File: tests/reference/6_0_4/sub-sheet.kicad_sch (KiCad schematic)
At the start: 7 parts, among them U1 74LS04

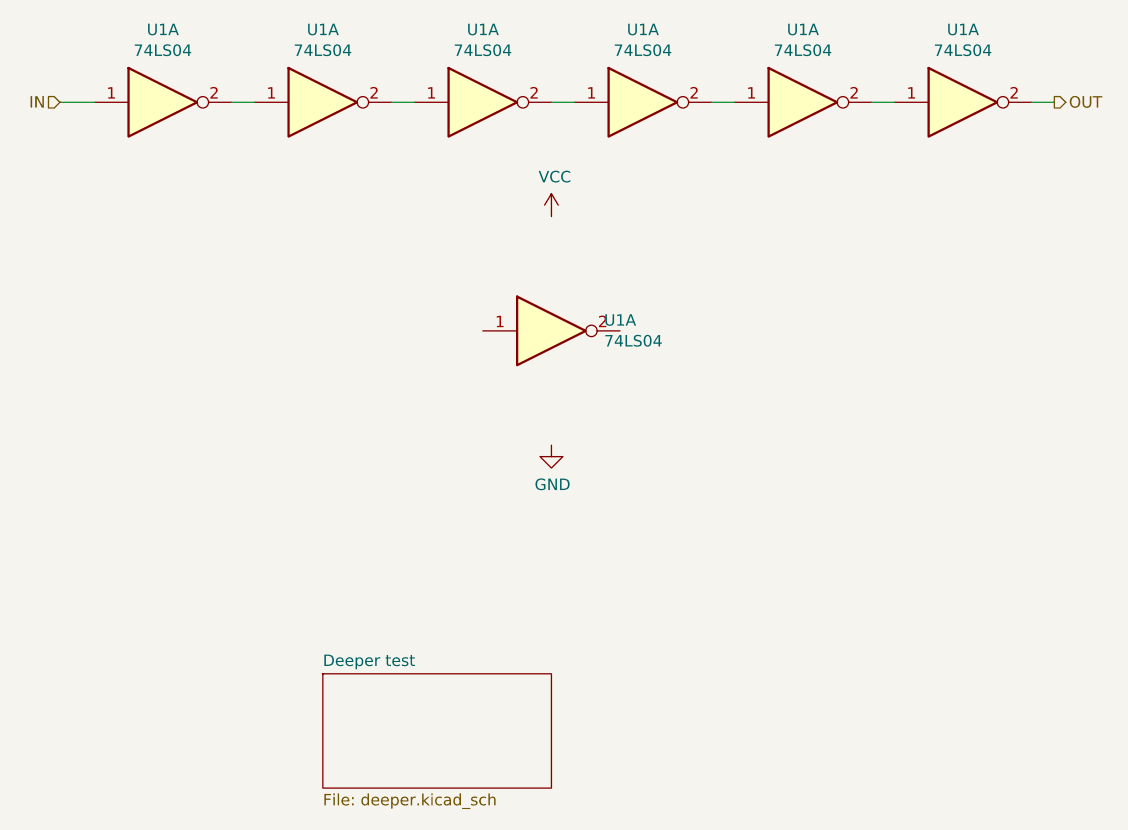
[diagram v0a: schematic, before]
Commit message: Added more KiCad SCH tests
- Qubic bezier
- Alternate pin
- Convert (DeMorgan)
- fields_autoplaced
- Bitmap scale
- Paper "user" & orientation
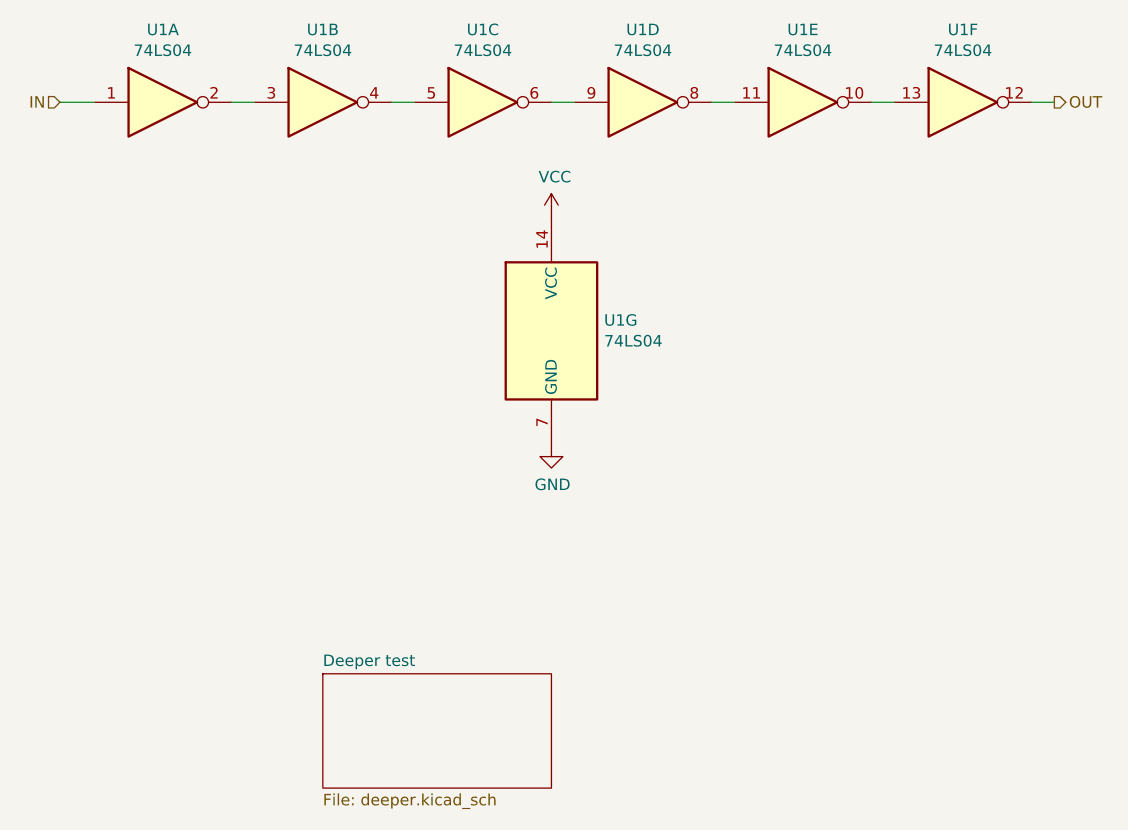
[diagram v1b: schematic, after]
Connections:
- net GND: now also U1.7 (GND)
- net OUT: now also U1.12; no longer U1.2
- net VCC: now also U1.14 (VCC)
- net at U1.2: now also U1.3; no longer U1.1
- new net: U1.4, U1.5
- new net: U1.6, U1.9
- new net: U1.11, U1.8
- new net: U1.10, U1.13
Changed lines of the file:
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@@
 (kicad_sch (version 20211123) (generator eeschema)
-  (paper "A4")
-  (title_block
-  )
+  (paper "User" 297.002 210.007)
   (wire (pts (xy 104.14 63.5) (xy 106.68 63.5))
     (stroke (width 0) (type default) (color 0 0 0 0))
@@
     (effects (font (size 1.27 1.27)) (justify left))
   )
-  (symbol (lib_id "74xx:74LS04") (at 96.52 63.5 0)
+  (symbol (lib_id "74xx:74LS04") (at 96.52 63.5 0) (unit 1)
     (in_bom yes) (on_board yes)
     (property "Reference" "U1" (id 0) (at 96.52 55.4482 0))
@@
     (pin "1")
     (pin "2")
-  )
-  (symbol (lib_id "74xx:74LS04") (at 114.3 63.5 0)
+    (pin "3")
+    (pin "4")
+    (pin "5")
+    (pin "6")
+    (pin "8")
+    (pin "9")
+    (pin "10")
+    (pin "11")
+    (pin "12")
+    (pin "13")
+    (pin "14")
+    (pin "7")
+  )
+  (symbol (lib_id "74xx:74LS04") (at 114.3 63.5 0) (unit 2)
     (in_bom yes) (on_board yes)
     (property "Reference" "U1" (id 0) (at 114.3 55.4482 0))
@@
       (effects (font (size 1.27 1.27)) hide)
     )
-    (pin "3")
-    (pin "4")
-  )
-  (symbol (lib_id "74xx:74LS04") (at 132.08 63.5 0)
+    (pin "1")
+    (pin "2")
+    (pin "3")
+    (pin "4")
+    (pin "5")
+    (pin "6")
+    (pin "8")
+    (pin "9")
+    (pin "10")
+    (pin "11")
+    (pin "12")
+    (pin "13")
+    (pin "14")
+    (pin "7")
+  )
+  (symbol (lib_id "74xx:74LS04") (at 132.08 63.5 0) (unit 3)
     (in_bom yes) (on_board yes)
     (property "Reference" "U1" (id 0) (at 132.08 55.4482 0))
@@
       (effects (font (size 1.27 1.27)) hide)
     )
-    (pin "5")
-    (pin "6")
-  )
-  (symbol (lib_id "74xx:74LS04") (at 149.86 63.5 0)
+    (pin "1")
+    (pin "2")
+    (pin "3")
+    (pin "4")
+    (pin "5")
+    (pin "6")
+    (pin "8")
+    (pin "9")
+    (pin "10")
+    (pin "11")
+    (pin "12")
+    (pin "13")
+    (pin "14")
+    (pin "7")
+  )
+  (symbol (lib_id "74xx:74LS04") (at 149.86 63.5 0) (unit 4)
     (in_bom yes) (on_board yes)
     (property "Reference" "U1" (id 0) (at 149.86 55.4482 0))
@@
       (effects (font (size 1.27 1.27)) hide)
     )
-    (pin "8")
-    (pin "9")
-  )
-  (symbol (lib_id "74xx:74LS04") (at 167.64 63.5 0)
+    (pin "1")
+    (pin "2")
+    (pin "3")
+    (pin "4")
+    (pin "5")
+    (pin "6")
+    (pin "8")
+    (pin "9")
+    (pin "10")
+    (pin "11")
+    (pin "12")
+    (pin "13")
+    (pin "14")
+    (pin "7")
+  )
+  (symbol (lib_id "74xx:74LS04") (at 167.64 63.5 0) (unit 5)
     (in_bom yes) (on_board yes)
     (property "Reference" "U1" (id 0) (at 167.64 55.4482 0))
@@
       (effects (font (size 1.27 1.27)) hide)
     )
-    (pin "10")
-    (pin "11")
-  )
-  (symbol (lib_id "74xx:74LS04") (at 185.42 63.5 0)
+    (pin "1")
+    (pin "2")
+    (pin "3")
+    (pin "4")
+    (pin "5")
+    (pin "6")
+    (pin "8")
+    (pin "9")
+    (pin "10")
+    (pin "11")
+    (pin "12")
+    (pin "13")
+    (pin "14")
+    (pin "7")
+  )
+  (symbol (lib_id "74xx:74LS04") (at 185.42 63.5 0) (unit 6)
     (in_bom yes) (on_board yes)
     (property "Reference" "U1" (id 0) (at 185.42 55.4482 0))
@@
       (effects (font (size 1.27 1.27)) hide)
     )
-    (pin "12")
-    (pin "13")
-  )
-  (symbol (lib_id "74xx:74LS04") (at 139.7 88.9 0)
+    (pin "1")
+    (pin "2")
+    (pin "3")
+    (pin "4")
+    (pin "5")
+    (pin "6")
+    (pin "8")
+    (pin "9")
+    (pin "10")
+    (pin "11")
+    (pin "12")
+    (pin "13")
+    (pin "14")
+    (pin "7")
+  )
+  (symbol (lib_id "74xx:74LS04") (at 139.7 88.9 0) (unit 7)
     (in_bom yes) (on_board yes)
     (property "Reference" "U1" (id 0) (at 145.542 87.7316 0)
@@
       (effects (font (size 1.27 1.27)) hide)
     )
-    (pin "14")
-    (pin "7")
-  )
-  (symbol (lib_id "power:VCC") (at 139.7 76.2 0)
+    (pin "1")
+    (pin "2")
+    (pin "3")
+    (pin "4")
+    (pin "5")
+    (pin "6")
+    (pin "8")
+    (pin "9")
+    (pin "10")
+    (pin "11")
+    (pin "12")
+    (pin "13")
+    (pin "14")
+    (pin "7")
+  )
+  (symbol (lib_id "power:VCC") (at 139.7 76.2 0) (unit 1)
     (in_bom yes) (on_board yes)
     (property "Reference" "#PWR?" (id 0) (at 139.7 80.01 0)
@@
     (pin "1")
   )
-  (symbol (lib_id "power:GND") (at 139.7 101.6 0)
+  (symbol (lib_id "power:GND") (at 139.7 101.6 0) (unit 1)
     (in_bom yes) (on_board yes)
     (property "Reference" "#PWR?" (id 0) (at 139.7 107.95 0)
